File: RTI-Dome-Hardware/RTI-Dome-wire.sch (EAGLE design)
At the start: 33 parts, among them IC2 74LVC244

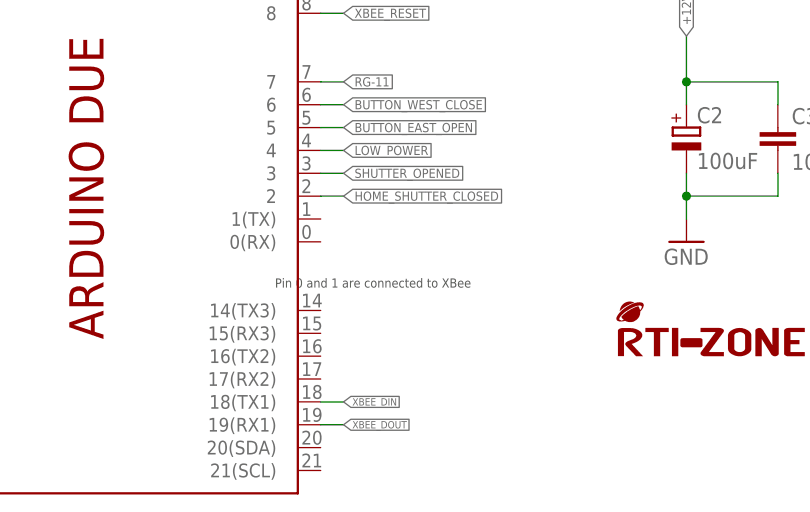
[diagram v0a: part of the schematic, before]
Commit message: Fix small error on schematics
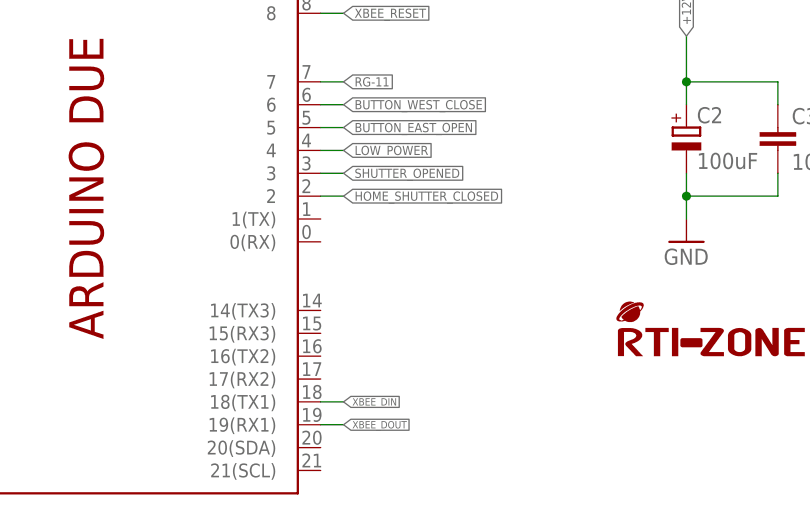
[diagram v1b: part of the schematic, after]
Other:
- note removed: "Pin 0 and 1 are connected to XBee"
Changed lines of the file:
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@@
 <sheet>
 <plain>
-<text x="129.54" y="35.56" size="1.016" layer="97">Pin 0 and 1 are connected to XBee</text>
 </plain>
 <instances>

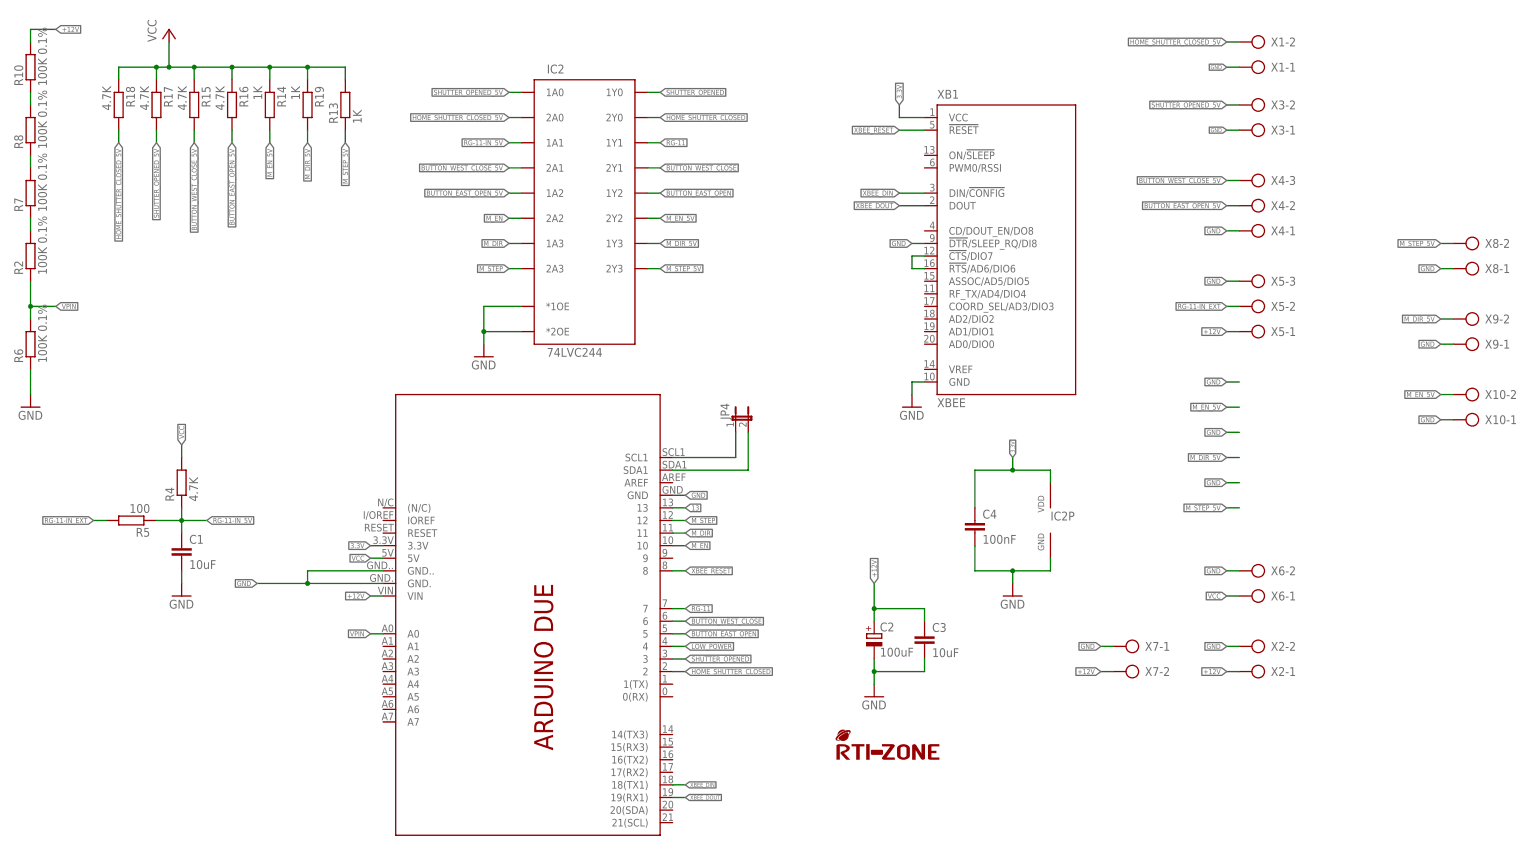
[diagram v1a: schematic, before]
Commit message: Stop interrupt in motor disable code.
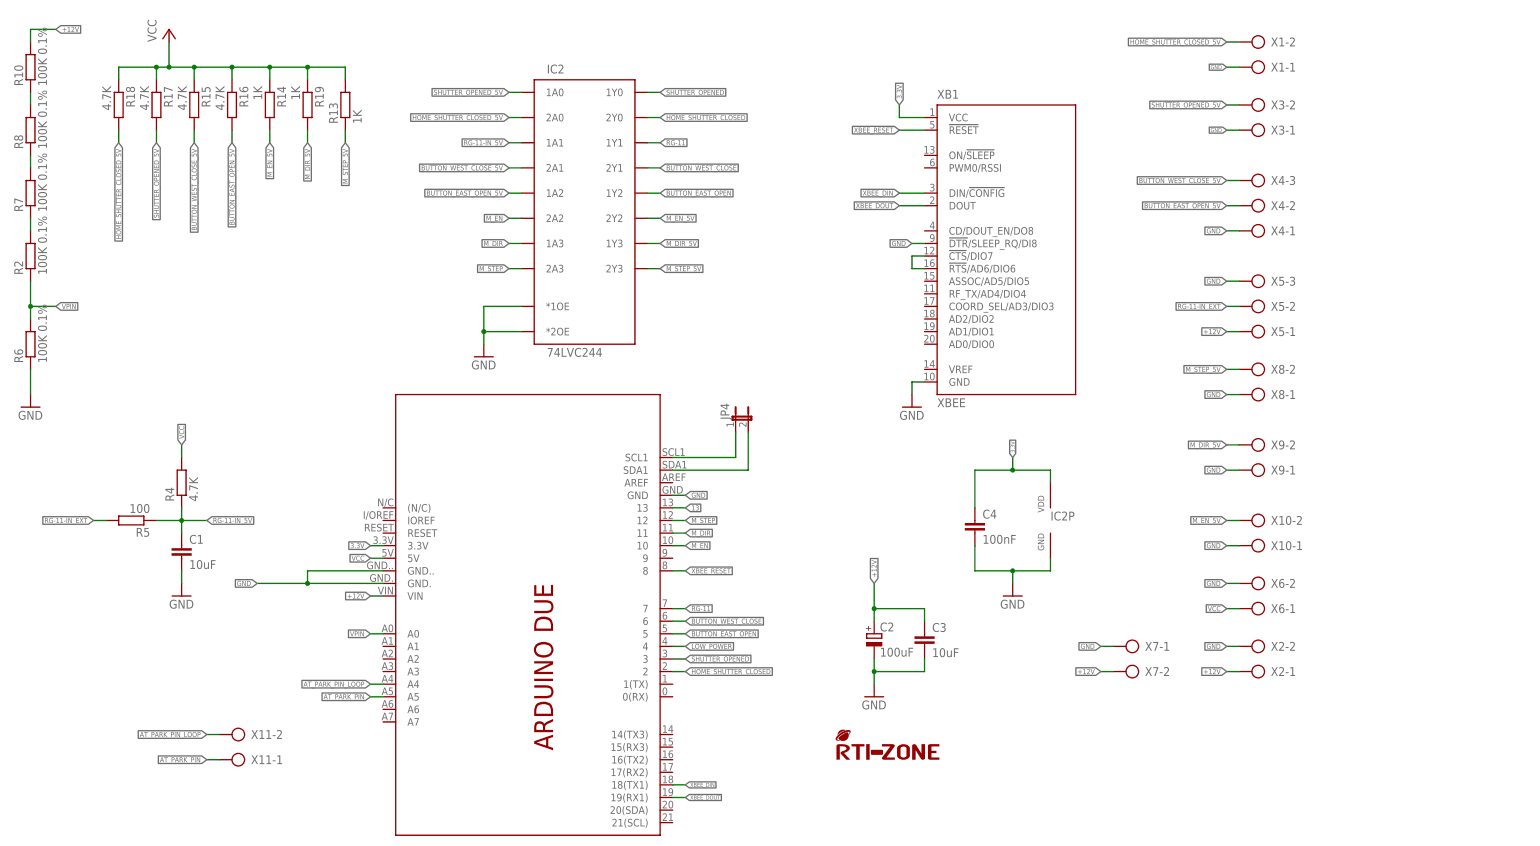
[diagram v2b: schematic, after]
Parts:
- added X11: (no value), con-ptr500:AK500/2
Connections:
- new net AT_PARK_PIN: PCB1.A5, X11-1.KL
- new net AT_PARK_PIN_LOOP: PCB1.A4, X11-2.KL
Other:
- moved on the sheet: X10-1, X10-2, X6-1, X6-2, X8-1, X8-2, X9-1, X9-2
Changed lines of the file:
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@@
 <part name="X9" library="con-ptr500" deviceset="AK500/2" device=""/>
 <part name="X10" library="con-ptr500" deviceset="AK500/2" device=""/>
+<part name="X11" library="con-ptr500" deviceset="AK500/2" device=""/>
 </parts>
 <sheets>
@@
 <instance part="XB1" gate="G$1" x="200.66" y="132.08"/>
 <instance part="GND6" gate="1" x="182.88" y="99.06"/>
-<instance part="X6" gate="-1" x="254" y="60.96" rot="R180"/>
-<instance part="X6" gate="-2" x="254" y="66.04" rot="R180"/>
+<instance part="X6" gate="-1" x="254" y="58.42" rot="R180"/>
+<instance part="X6" gate="-2" x="254" y="63.5" rot="R180"/>
 <instance part="PCB1" gate="G$1" x="106.68" y="45.72" rot="R270"/>
 <instance part="R2" gate="G$1" x="5.08" y="129.54" rot="R90"/>
@@
 <instance part="X7" gate="-1" x="228.6" y="50.8" rot="R180"/>
 <instance part="X7" gate="-2" x="228.6" y="45.72" rot="R180"/>
-<instance part="X8" gate="-1" x="297.18" y="127" rot="R180"/>
-<instance part="X8" gate="-2" x="297.18" y="132.08" rot="R180"/>
-<instance part="X9" gate="-1" x="297.18" y="111.76" rot="R180"/>
-<instance part="X9" gate="-2" x="297.18" y="116.84" rot="R180"/>
-<instance part="X10" gate="-1" x="297.18" y="96.52" rot="R180"/>
-<instance part="X10" gate="-2" x="297.18" y="101.6" rot="R180"/>
+<instance part="X8" gate="-1" x="254" y="101.6" rot="R180"/>
+<instance part="X8" gate="-2" x="254" y="106.68" rot="R180"/>
+<instance part="X9" gate="-1" x="254" y="86.36" rot="R180"/>
+<instance part="X9" gate="-2" x="254" y="91.44" rot="R180"/>
+<instance part="X10" gate="-1" x="254" y="71.12" rot="R180"/>
+<instance part="X10" gate="-2" x="254" y="76.2" rot="R180"/>
+<instance part="X11" gate="-1" x="48.26" y="27.94" rot="R180"/>
+<instance part="X11" gate="-2" x="48.26" y="33.02" rot="R180"/>
 </instances>
 <busses>
@@
 <pinref part="PCB1" gate="G$1" pin="GND."/>
 <pinref part="PCB1" gate="G$1" pin="GND.."/>
-</segment>
-<segment>
-<wire x1="246.38" y1="104.14" x2="248.92" y2="104.14" width="0.1524" layer="91"/>
-<label x="246.38" y="104.14" size="1.016" layer="95" rot="MR0" xref="yes"/>
-</segment>
-<segment>
-<wire x1="246.38" y1="93.98" x2="248.92" y2="93.98" width="0.1524" layer="91"/>
-<label x="246.38" y="93.98" size="1.016" layer="95" rot="MR0" xref="yes"/>
-</segment>
-<segment>
-<wire x1="246.38" y1="83.82" x2="248.92" y2="83.82" width="0.1524" layer="91"/>
-<label x="246.38" y="83.82" size="1.016" layer="95" rot="MR0" xref="yes"/>
 </segment>
 <segment>
@@
 </segment>
 <segment>
-<wire x1="246.38" y1="66.04" x2="248.92" y2="66.04" width="0.1524" layer="91"/>
-<label x="246.38" y="66.04" size="1.016" layer="95" rot="R180" xref="yes"/>
+<wire x1="246.38" y1="63.5" x2="248.92" y2="63.5" width="0.1524" layer="91"/>
+<label x="246.38" y="63.5" size="1.016" layer="95" rot="R180" xref="yes"/>
 <pinref part="X6" gate="-2" pin="KL"/>
 </segment>
 <segment>
 <pinref part="X8" gate="-1" pin="KL"/>
-<wire x1="289.56" y1="127" x2="292.1" y2="127" width="0.1524" layer="91"/>
-<label x="289.56" y="127" size="1.016" layer="95" rot="R180" xref="yes"/>
+<wire x1="246.38" y1="101.6" x2="248.92" y2="101.6" width="0.1524" layer="91"/>
+<label x="246.38" y="101.6" size="1.016" layer="95" rot="R180" xref="yes"/>
 </segment>
 <segment>
 <pinref part="X9" gate="-1" pin="KL"/>
-<wire x1="289.56" y1="111.76" x2="292.1" y2="111.76" width="0.1524" layer="91"/>
-<label x="289.56" y="111.76" size="1.016" layer="95" rot="R180" xref="yes"/>
+<wire x1="246.38" y1="86.36" x2="248.92" y2="86.36" width="0.1524" layer="91"/>
+<label x="246.38" y="86.36" size="1.016" layer="95" rot="R180" xref="yes"/>
 </segment>
 <segment>
 <pinref part="X10" gate="-1" pin="KL"/>
-<wire x1="289.56" y1="96.52" x2="292.1" y2="96.52" width="0.1524" layer="91"/>
-<label x="289.56" y="96.52" size="1.016" layer="95" rot="R180" xref="yes"/>
+<wire x1="246.38" y1="71.12" x2="248.92" y2="71.12" width="0.1524" layer="91"/>
+<label x="246.38" y="71.12" size="1.016" layer="95" rot="R180" xref="yes"/>
 </segment>
 </net>
@@
 <net name="M_STEP_5V" class="0">
 <segment>
-<wire x1="246.38" y1="78.74" x2="248.92" y2="78.74" width="0.1524" layer="91"/>
-<label x="246.38" y="78.74" size="1.016" layer="95" rot="MR0" xref="yes"/>
-</segment>
-<segment>
 <wire x1="68.58" y1="152.4" x2="68.58" y2="154.94" width="0.1524" layer="91"/>
 <label x="68.58" y="152.4" size="1.016" layer="95" rot="R270" xref="yes"/>
@@
 <segment>
 <pinref part="X8" gate="-2" pin="KL"/>
-<wire x1="289.56" y1="132.08" x2="292.1" y2="132.08" width="0.1524" layer="91"/>
-<label x="289.56" y="132.08" size="1.016" layer="95" rot="R180" xref="yes"/>
+<wire x1="246.38" y1="106.68" x2="248.92" y2="106.68" width="0.1524" layer="91"/>
+<label x="246.38" y="106.68" size="1.016" layer="95" rot="R180" xref="yes"/>
 </segment>
 </net>
 <net name="M_DIR_5V" class="0">
-<segment>
-<wire x1="246.38" y1="88.9" x2="248.92" y2="88.9" width="0.1524" layer="91"/>
-<label x="246.38" y="88.9" size="1.016" layer="95" rot="MR0" xref="yes"/>
-</segment>
 <segment>
 <label x="60.96" y="152.4" size="1.016" layer="95" rot="R270" xref="yes"/>
@@
 <segment>
 <pinref part="X9" gate="-2" pin="KL"/>
-<wire x1="289.56" y1="116.84" x2="292.1" y2="116.84" width="0.1524" layer="91"/>
-<label x="289.56" y="116.84" size="1.016" layer="95" rot="R180" xref="yes"/>
+<wire x1="246.38" y1="91.44" x2="248.92" y2="91.44" width="0.1524" layer="91"/>
+<label x="246.38" y="91.44" size="1.016" layer="95" rot="R180" xref="yes"/>
 </segment>
 </net>
 <net name="M_EN_5V" class="0">
-<segment>
-<wire x1="246.38" y1="99.06" x2="248.92" y2="99.06" width="0.1524" layer="91"/>
-<label x="246.38" y="99.06" size="1.016" layer="95" rot="MR0" xref="yes"/>
-</segment>
 <segment>
 <label x="53.34" y="152.4" size="1.016" layer="95" rot="R270" xref="yes"/>
@@
 <segment>
 <pinref part="X10" gate="-2" pin="KL"/>
-<wire x1="289.56" y1="101.6" x2="292.1" y2="101.6" width="0.1524" layer="91"/>
-<label x="289.56" y="101.6" size="1.016" layer="95" rot="R180" xref="yes"/>
+<wire x1="246.38" y1="76.2" x2="248.92" y2="76.2" width="0.1524" layer="91"/>
+<label x="246.38" y="76.2" size="1.016" layer="95" rot="R180" xref="yes"/>
 </segment>
 </net>
@@
 </segment>
 <segment>
-<wire x1="246.38" y1="60.96" x2="248.92" y2="60.96" width="0.1524" layer="91"/>
-<label x="246.38" y="60.96" size="1.016" layer="95" rot="R180" xref="yes"/>
+<wire x1="246.38" y1="58.42" x2="248.92" y2="58.42" width="0.1524" layer="91"/>
+<label x="246.38" y="58.42" size="1.016" layer="95" rot="R180" xref="yes"/>
 <pinref part="X6" gate="-1" pin="KL"/>
 </segment>
@@
 </segment>
 </net>
+<net name="AT_PARK_PIN_LOOP" class="0">
+<segment>
+<pinref part="X11" gate="-2" pin="KL"/>
+<wire x1="40.64" y1="33.02" x2="43.18" y2="33.02" width="0.1524" layer="91"/>
+<label x="40.64" y="33.02" size="1.016" layer="95" rot="R180" xref="yes"/>
+</segment>
+<segment>
+<wire x1="73.66" y1="43.18" x2="76.2" y2="43.18" width="0.1524" layer="91"/>
+<label x="73.66" y="43.18" size="1.016" layer="95" rot="R180" xref="yes"/>
+<pinref part="PCB1" gate="G$1" pin="A4"/>
+</segment>
+</net>
+<net name="AT_PARK_PIN" class="0">
+<segment>
+<pinref part="X11" gate="-1" pin="KL"/>
+<wire x1="40.64" y1="27.94" x2="43.18" y2="27.94" width="0.1524" layer="91"/>
+<label x="40.64" y="27.94" size="1.016" layer="95" rot="R180" xref="yes"/>
+</segment>
+<segment>
+<wire x1="73.66" y1="40.64" x2="76.2" y2="40.64" width="0.1524" layer="91"/>
+<label x="73.66" y="40.64" size="1.016" layer="95" rot="R180" xref="yes"/>
+<pinref part="PCB1" gate="G$1" pin="A5"/>
+</segment>
+</net>
